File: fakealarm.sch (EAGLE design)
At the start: 16 parts, among them IC1 LTC555, Q1 2N7000, Q2 2N7000, X1 RUN, X2 BAT, X3 GND, X4 +, X5 LED

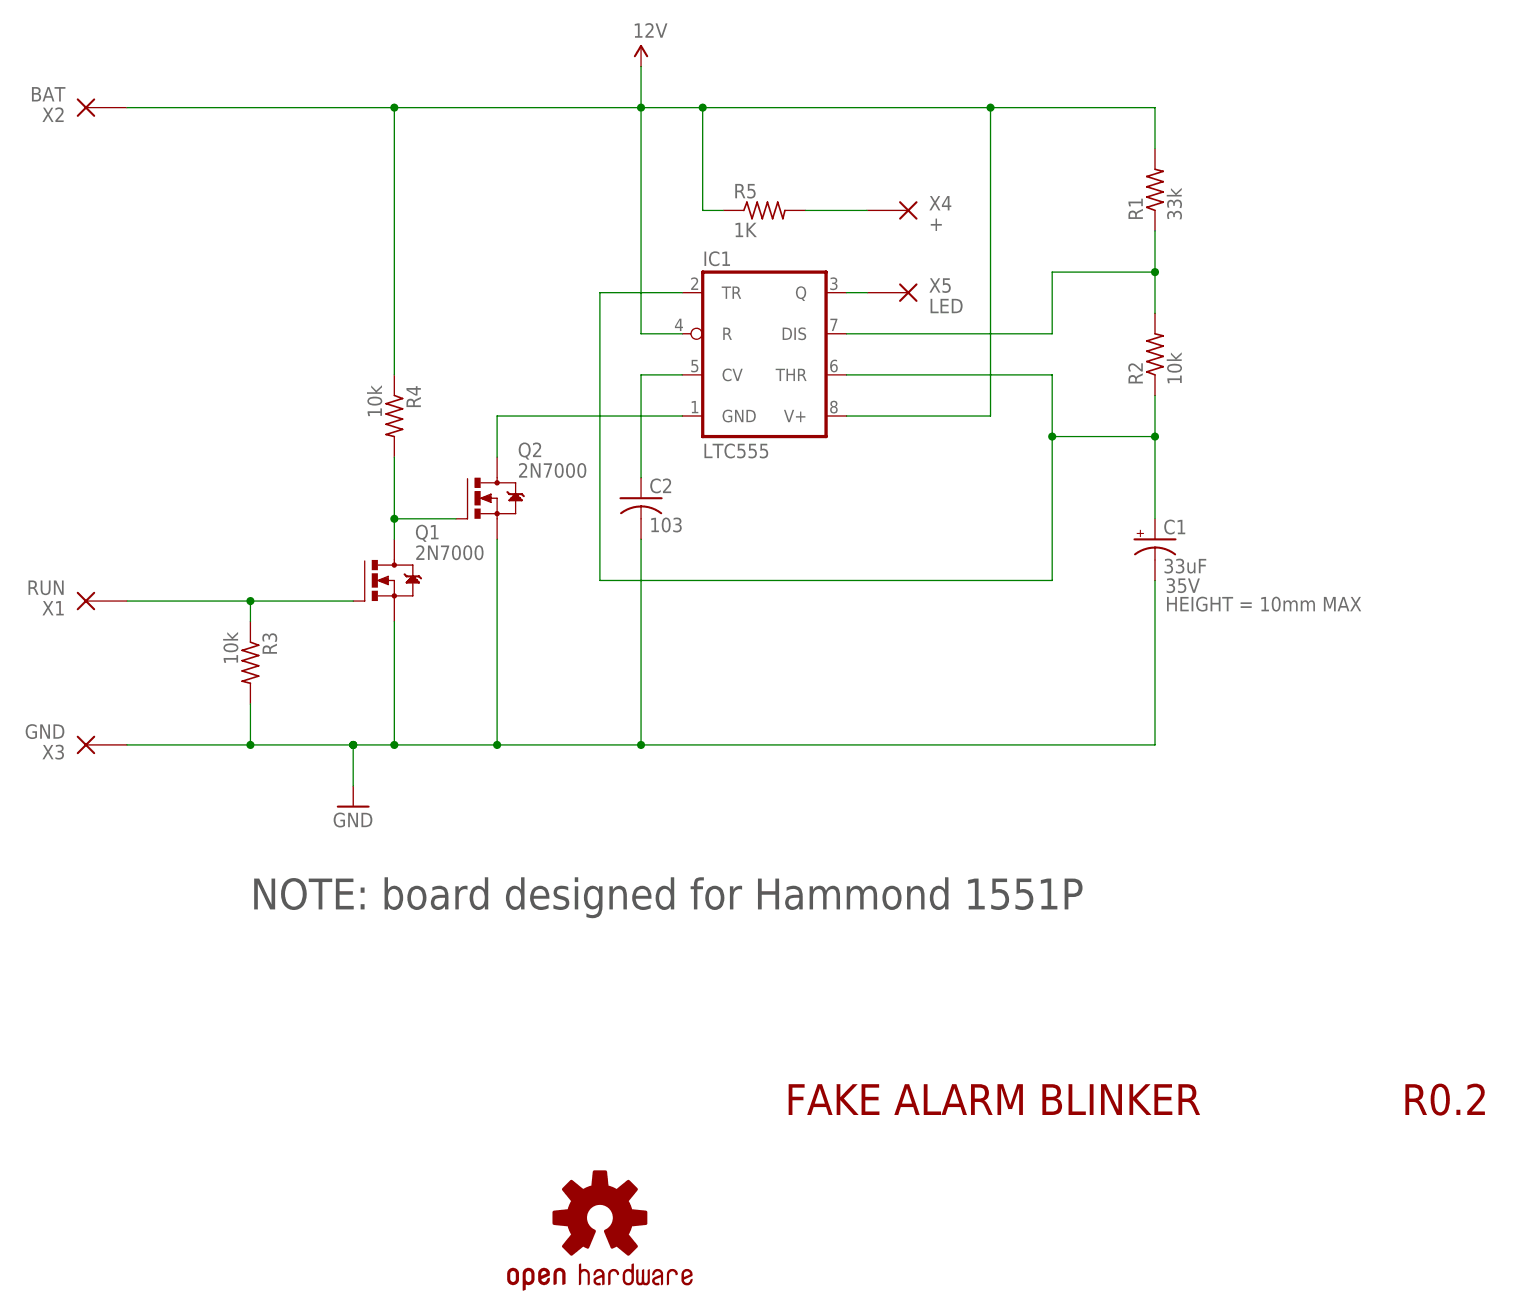
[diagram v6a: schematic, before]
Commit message: Layout tweaks on board and schematic. Added reverse protection diode
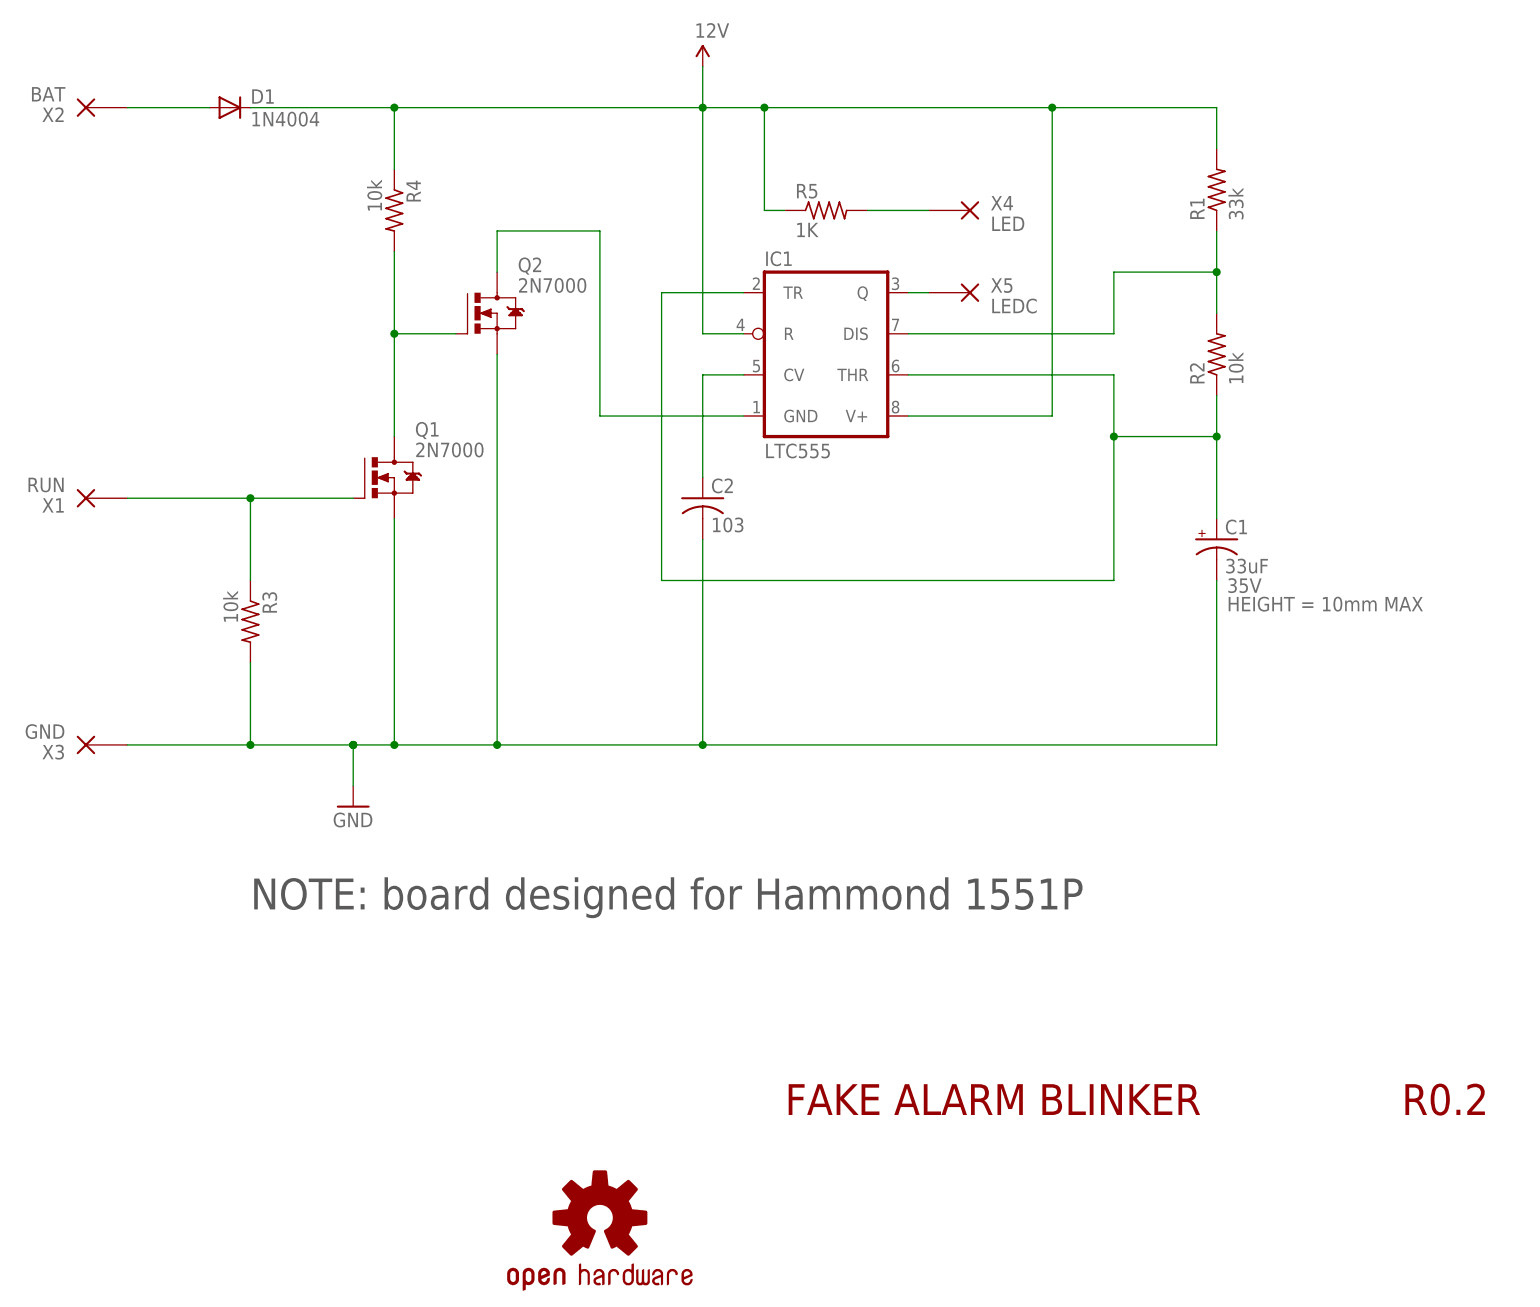
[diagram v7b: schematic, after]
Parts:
- added D1: 1N4004, diode:1N4004
- X4: value + -> LED
- X5: value LED -> LEDC
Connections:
- new net N$6: D1.A, X2.P
- net 12V: now also D1.C; no longer X2.P
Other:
- moved on the sheet: C1, C2, IC1, Q1, Q2, R1, R2, R3, R4, R5, X1, X4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
